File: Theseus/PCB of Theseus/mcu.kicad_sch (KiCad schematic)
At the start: 23 parts, among them J3 CN4 STDC14 (Programmer), U3 STM32H750VBTx, U4 MX25L25645G, Y1 ASE-4.000MHz-L-C-T

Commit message: Changed the schematic to accommodate four 4-wire PTs
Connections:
- net PT4+: now reaches U3.32 (PC4)
- net PT4-: now reaches U3.33 (PC5)
- net PT4 renamed PT2-
- net PT5 renamed PT2+
- net PT6 renamed PT1-
- net PT_1 renamed PT3+
- net PT_2 renamed PT3-
- net PT_3 renamed PT1+
- no-connect marks 49 -> 47
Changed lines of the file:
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@@
-	)
-	(no_connect
-		(at 102.87 148.59)
 	)
 	(no_connect
@@
 	)
 	(no_connect
+		(at 102.87 92.71)
+	)
+	(no_connect
 		(at 57.15 102.87)
 	)
@@
 	)
 	(no_connect
-		(at 102.87 146.05)
-	)
-	(no_connect
 		(at 57.15 100.33)
 	)
@@
 	(no_connect
 		(at 57.15 133.35)
-	)
-	(no_connect
-		(at 102.87 92.71)
 	)
 	(no_connect
@@
 		)
 	)
-	(hierarchical_label "PT6"
+	(hierarchical_label "PT1-"
 		(shape input)
 		(at 102.87 52.07 0)
+		(effects
+			(font
+				(size 1.27 1.27)
+			)
+			(justify left)
+		)
+	)
+	(hierarchical_label "PT4-"
+		(shape input)
+		(at 102.87 148.59 0)
 		(effects
 			(font
@@
 		)
 	)
-	(hierarchical_label "PT_1"
+	(hierarchical_label "PT3+"
 		(shape input)
 		(at 102.87 140.97 0)
@@
 		)
 	)
+	(hierarchical_label "PT4+"
+		(shape input)
+		(at 102.87 146.05 0)
+		(effects
+			(font
+				(size 1.27 1.27)
+			)
+			(justify left)
+		)
+	)
 	(hierarchical_label "HALL_2"
 		(shape input)
@@
 		)
 	)
-	(hierarchical_label "PT_2"
+	(hierarchical_label "PT3-"
 		(shape input)
 		(at 102.87 143.51 0)
@@
 		)
 	)
-	(hierarchical_label "PT4"
+	(hierarchical_label "PT2-"
 		(shape input)
 		(at 102.87 57.15 0)
@@
 		)
 	)
-	(hierarchical_label "PT_3"
+	(hierarchical_label "PT1+"
 		(shape input)
 		(at 102.87 49.53 0)
@@
 		)
 	)
-	(hierarchical_label "PT5"
+	(hierarchical_label "PT2+"
 		(shape input)
 		(at 102.87 54.61 0)

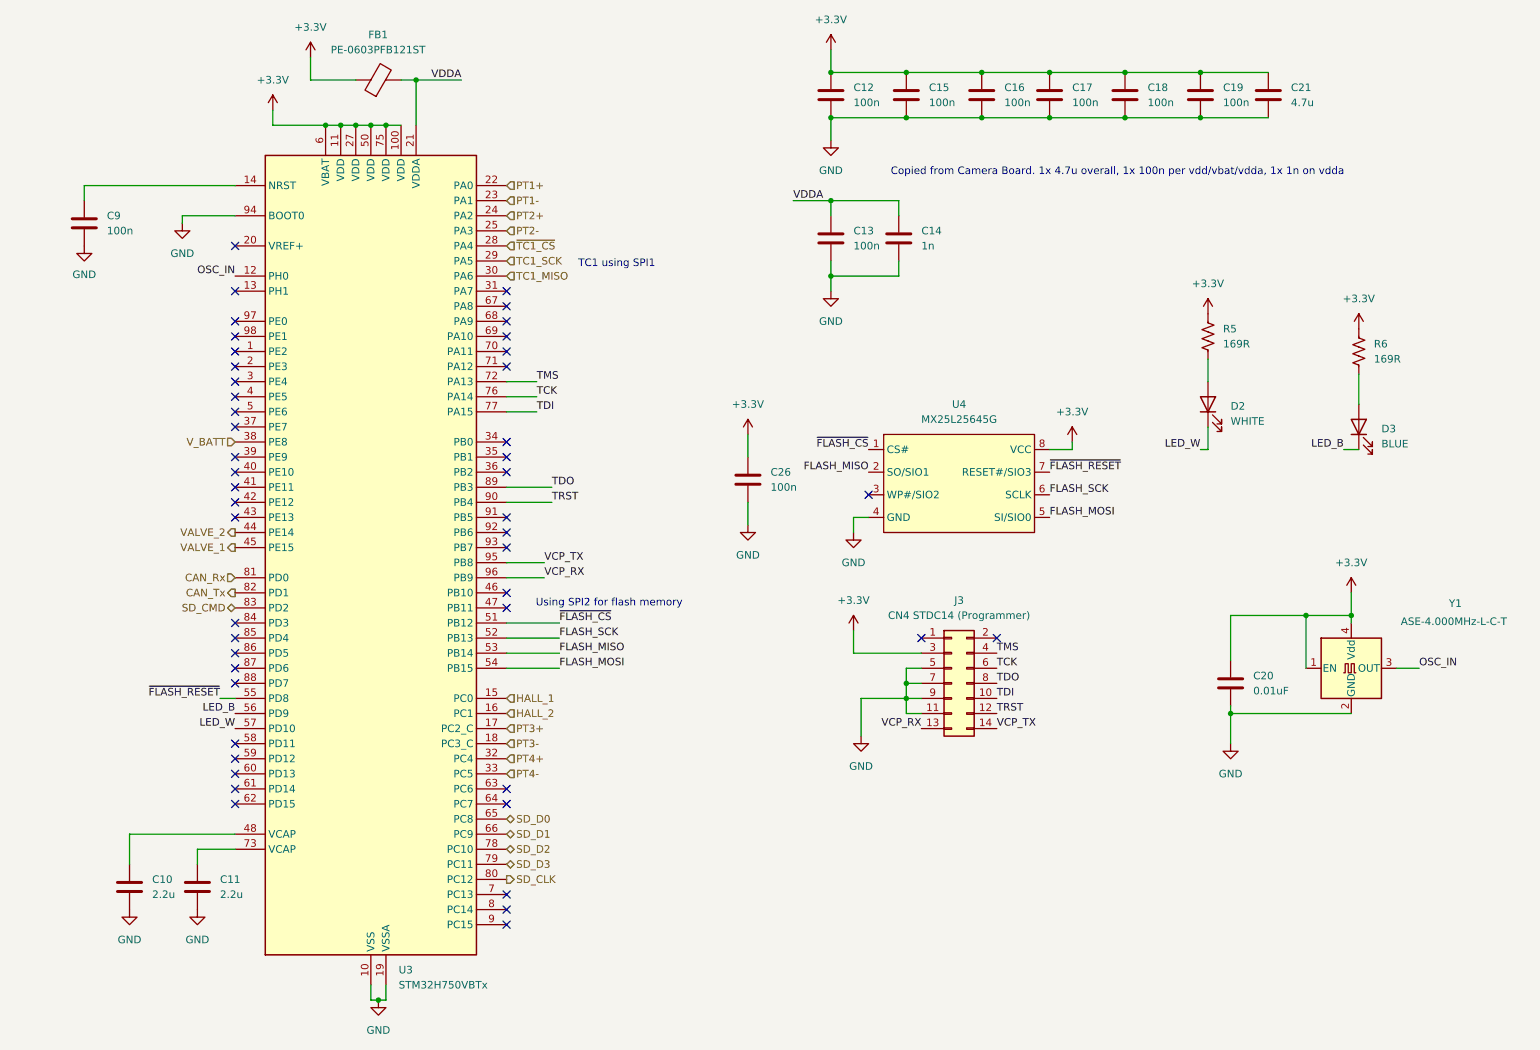
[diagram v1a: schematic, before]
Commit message: Swapped out the h7 STM to a H503RBT. Should have retained all pin functionality and tried to maintain physical pin positions so routing should be similar
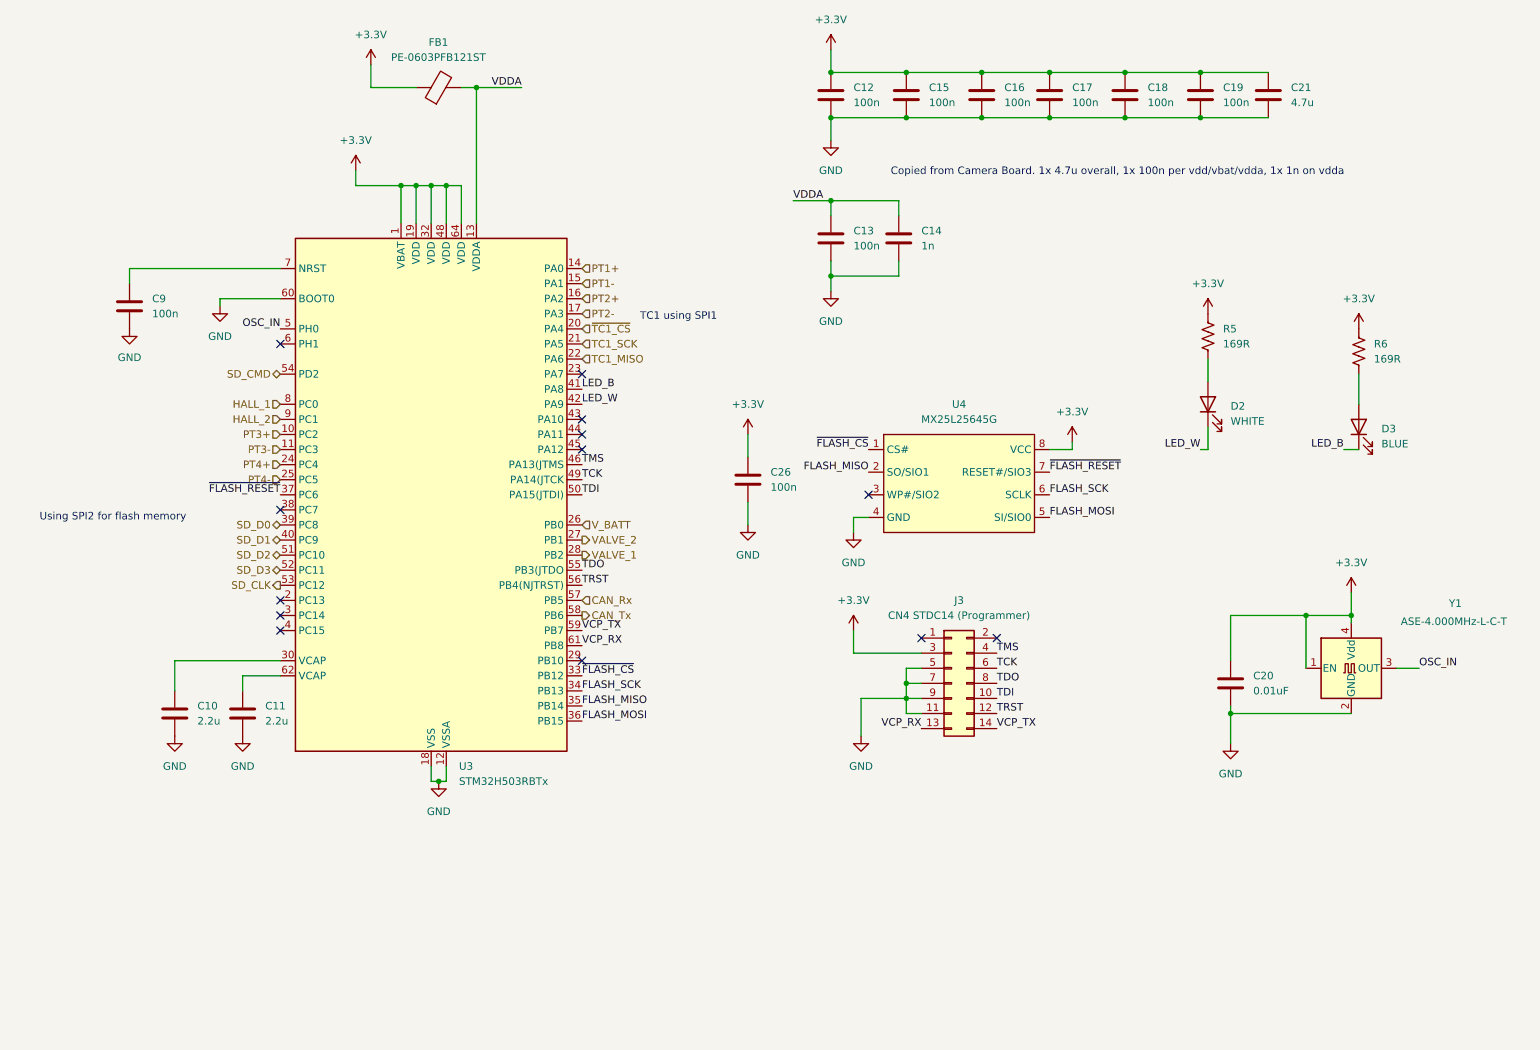
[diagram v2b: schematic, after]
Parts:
- removed U3: STM32H750VBTx, Package_QFP:LQFP-100_14x14mm_P0.5mm, symbol MCU_ST_STM32H7:STM32H750VBTx
- added U3: STM32H503RBTx, Package_QFP:LQFP-64_10x10mm_P0.5mm, symbol MCU_ST_STM32H5:STM32H503RBTx
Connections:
- net +3.3V: now also U3.1 (VBAT), U3.19 (VDD), U3.32 (VDD), U3.48 (VDD), U3.64 (VDD)
- net CAN_Rx: now also U3.57 (PB5)
- net CAN_Tx: now also U3.58 (PB6)
- net FLASH_MISO: now also U3.35 (PB14)
- net FLASH_MOSI: now also U3.36 (PB15)
- net FLASH_SCK: now also U3.34 (PB13)
- net GND: now also U3.12 (VSSA), U3.18 (VSS), U3.31 (VSS), U3.47 (VSS), U3.60 (BOOT0), U3.63 (VSS)
- net HALL_1: now also U3.8 (PC0)
- net HALL_2: now also U3.9 (PC1)
- net LED_B: now also U3.41 (PA8)
- net LED_W: now also U3.42 (PA9)
- net OSC_IN: now also U3.5 (PH0)
- net PT1+: now also U3.14 (PA0)
- net PT1-: now also U3.15 (PA1)
- net PT2+: now also U3.16 (PA2)
- net PT2-: now also U3.17 (PA3)
- net PT3+: now also U3.10 (PC2)
- net PT3-: now also U3.11 (PC3)
- net PT4+: now also U3.24 (PC4)
- net PT4-: now also U3.25 (PC5)
- net SD_CLK: now also U3.53 (PC12)
- net SD_CMD: now also U3.54 (PD2)
- net SD_D0: now also U3.39 (PC8)
- net SD_D1: now also U3.40 (PC9)
- net SD_D2: now also U3.51 (PC10)
- net SD_D3: now also U3.52 (PC11)
- net TC1_MISO: now also U3.22 (PA6)
- net TC1_SCK: now also U3.21 (PA5)
- net TCK: now also U3.49 (PA14(JTCK)
- net TDI: now also U3.50 (PA15(JTDI))
- net TDO: now also U3.55 (PB3(JTDO)
- net TMS: now also U3.46 (PA13(JTMS)
- net TRST: now also U3.56 (PB4(NJTRST))
- net VALVE_1: now also U3.28 (PB2)
- net VALVE_2: now also U3.27 (PB1)
- net VCP_RX: now also U3.61 (PB8)
- net VCP_TX: now also U3.59 (PB7)
- net VDDA: now also U3.13 (VDDA)
- net V_BATT: now also U3.26 (PB0)
- net ~{FLASH_CS}: now also U3.33 (PB12)
- net ~{FLASH_RESET}: now also U3.37 (PC6)
- net ~{TC1_CS}: now also U3.20 (PA4)
- net at C10.1: now also U3.30 (VCAP)
- net at C9.1: now also U3.7 (NRST)
- net at C11.1: now also U3.62 (VCAP)
- no-connect marks 47 -> 13
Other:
- moved on the sheet: C10, C11, C9, FB1

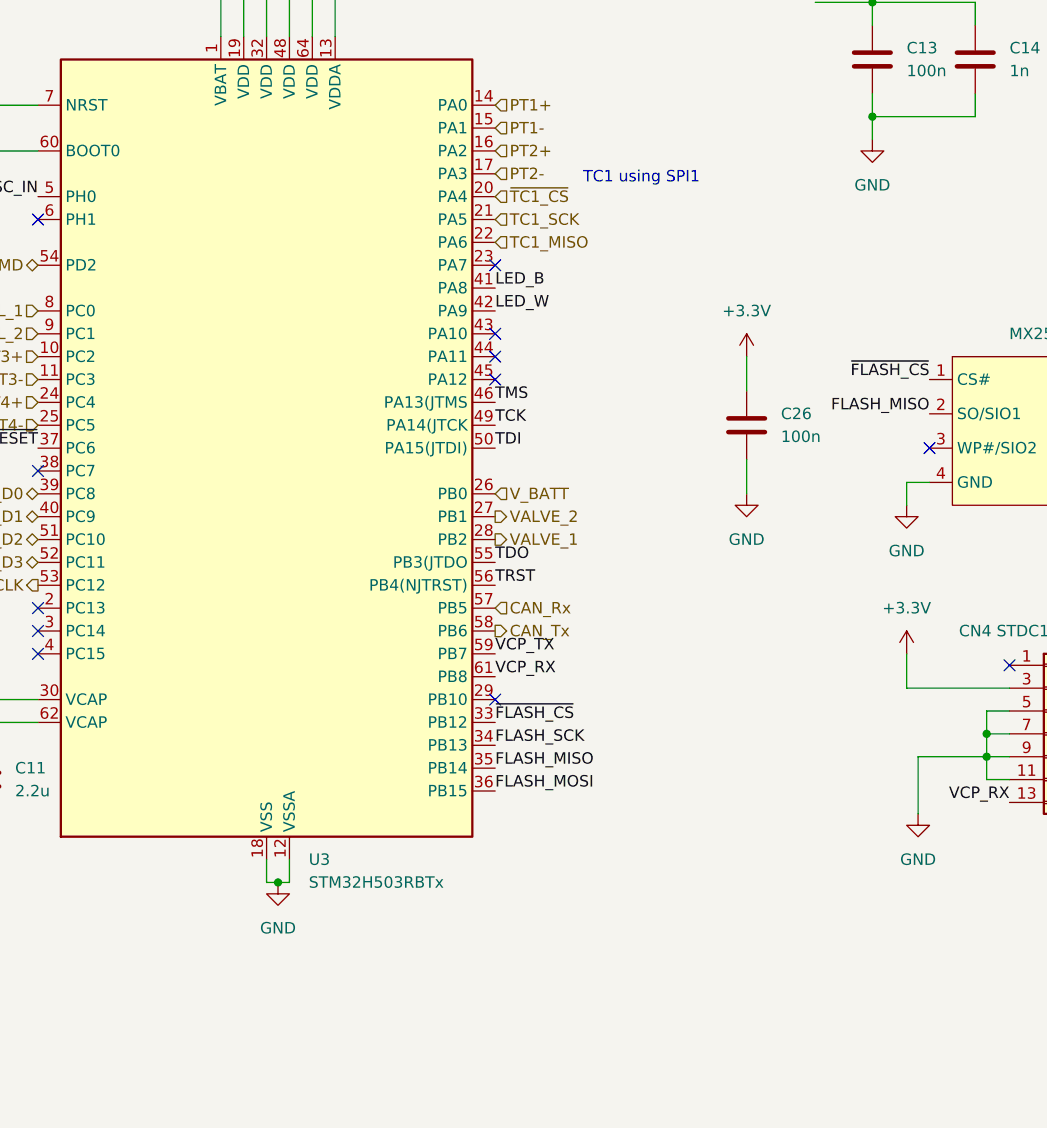
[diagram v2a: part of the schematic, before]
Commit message: Added an entirely new file for the thermocouple in accordance with Jason H's design of a cheaper thermocouple circuit Also swapped out the STM H7 for a H5 with 64 pins. Everything should work fine but someone could confirm this if they have lots of free time
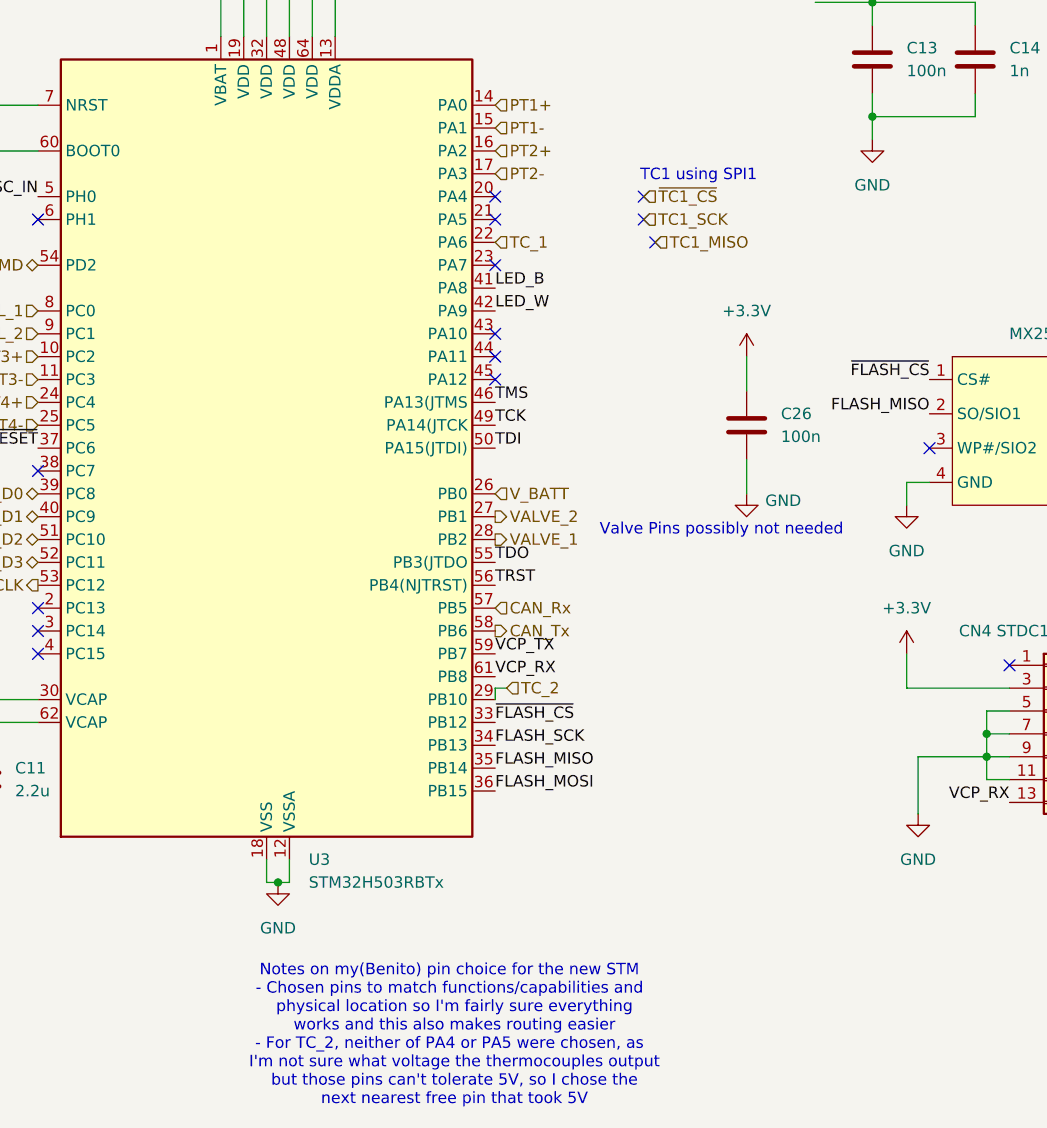
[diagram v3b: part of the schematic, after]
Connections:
- net TC1_MISO: no longer U3.22 (PA6)
- net TC1_SCK: no longer U3.21 (PA5)
- net ~{TC1_CS}: no longer U3.20 (PA4)
- net TC_2: now reaches U3.29 (PB10)
- new net TC_1: U3.22 (PA6)
- no-connect marks 13 -> 17
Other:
- note added: "Notes on my(Benito) pin choice for the new STM - Chosen pins to match functions/capabilities and physical location so I'm fairly sure everything works and this also makes routing easier - For TC_2, neither of PA4 or PA5 were chosen, as I'm not sure what voltage the thermocouples output but those pins can't tolerate 5V, so I chose the next nearest free pin that took 5V"
- note added: "Valve Pins possibly not needed"
